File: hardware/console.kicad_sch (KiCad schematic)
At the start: 56 parts, among them J1 USB-C_Module, J3 SWD, J4 UART, J5 LiPo_140mAh, SW1 SW_LEFT, SW10 SW_BOOT0, SW2 SW_RIGHT, SW3 SW_UP, SW4 SW_DOWN, SW5 SW_A, SW6 SW_B, SW7 SW_POWER, SW8 SW_START, SW9 SW_SELECT, U1 STM32G0B1CBT6, U2 XC6206P332MR, U3 TP4054

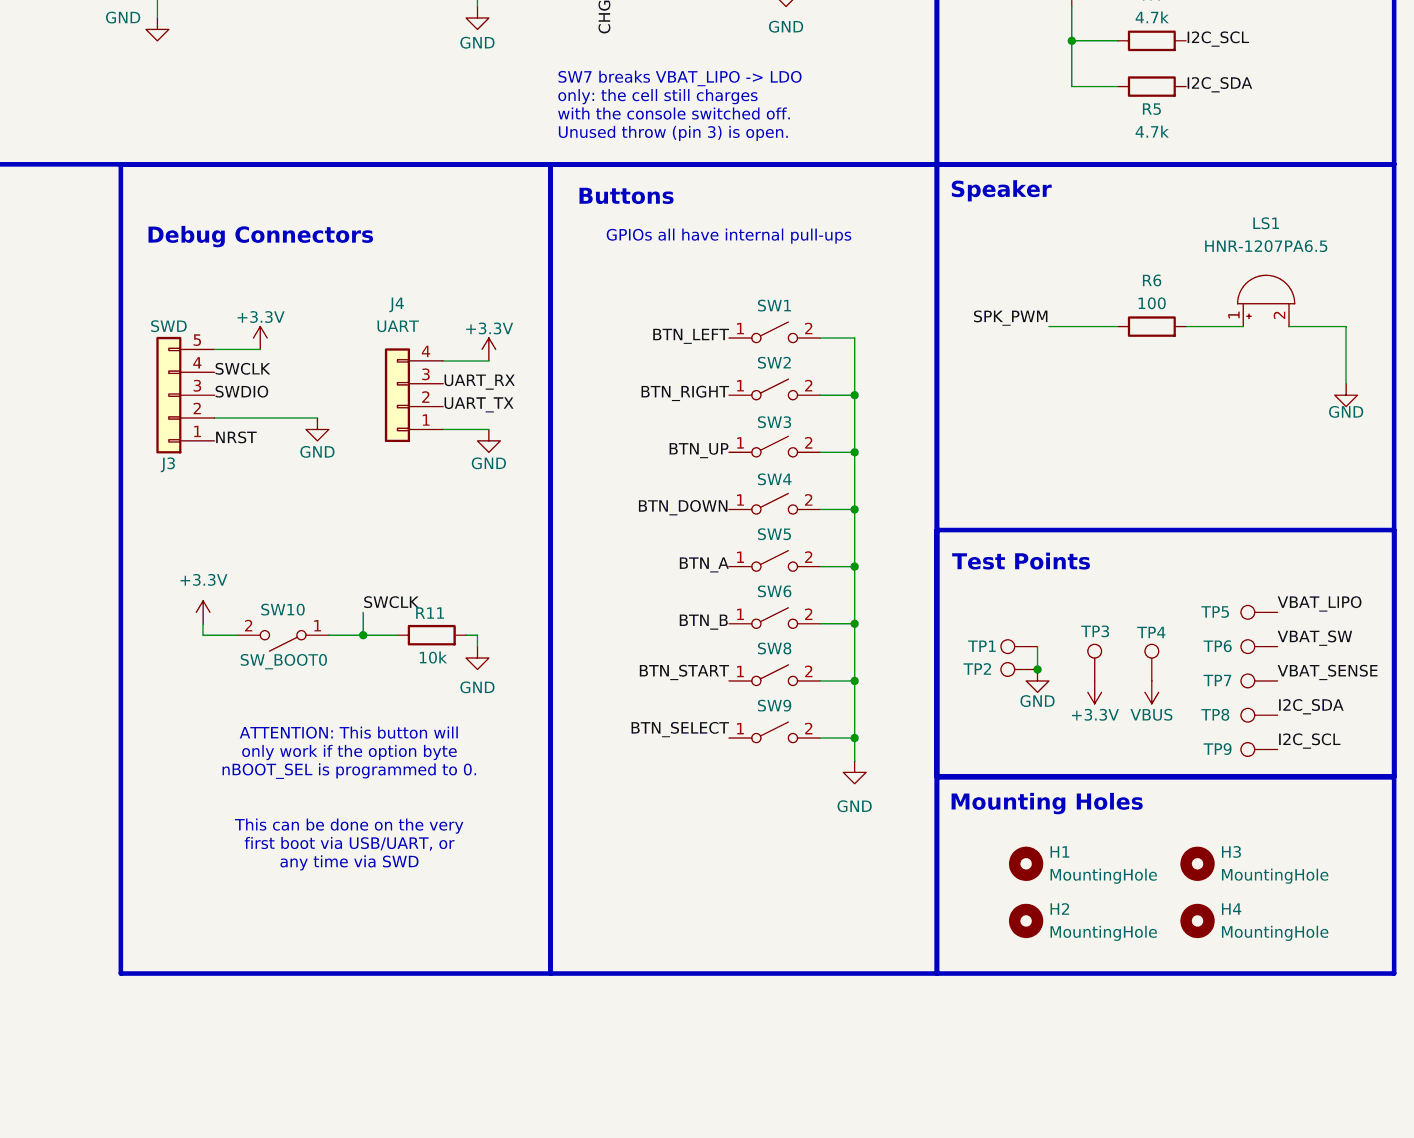
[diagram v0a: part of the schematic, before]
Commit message: remove the boot0 btn
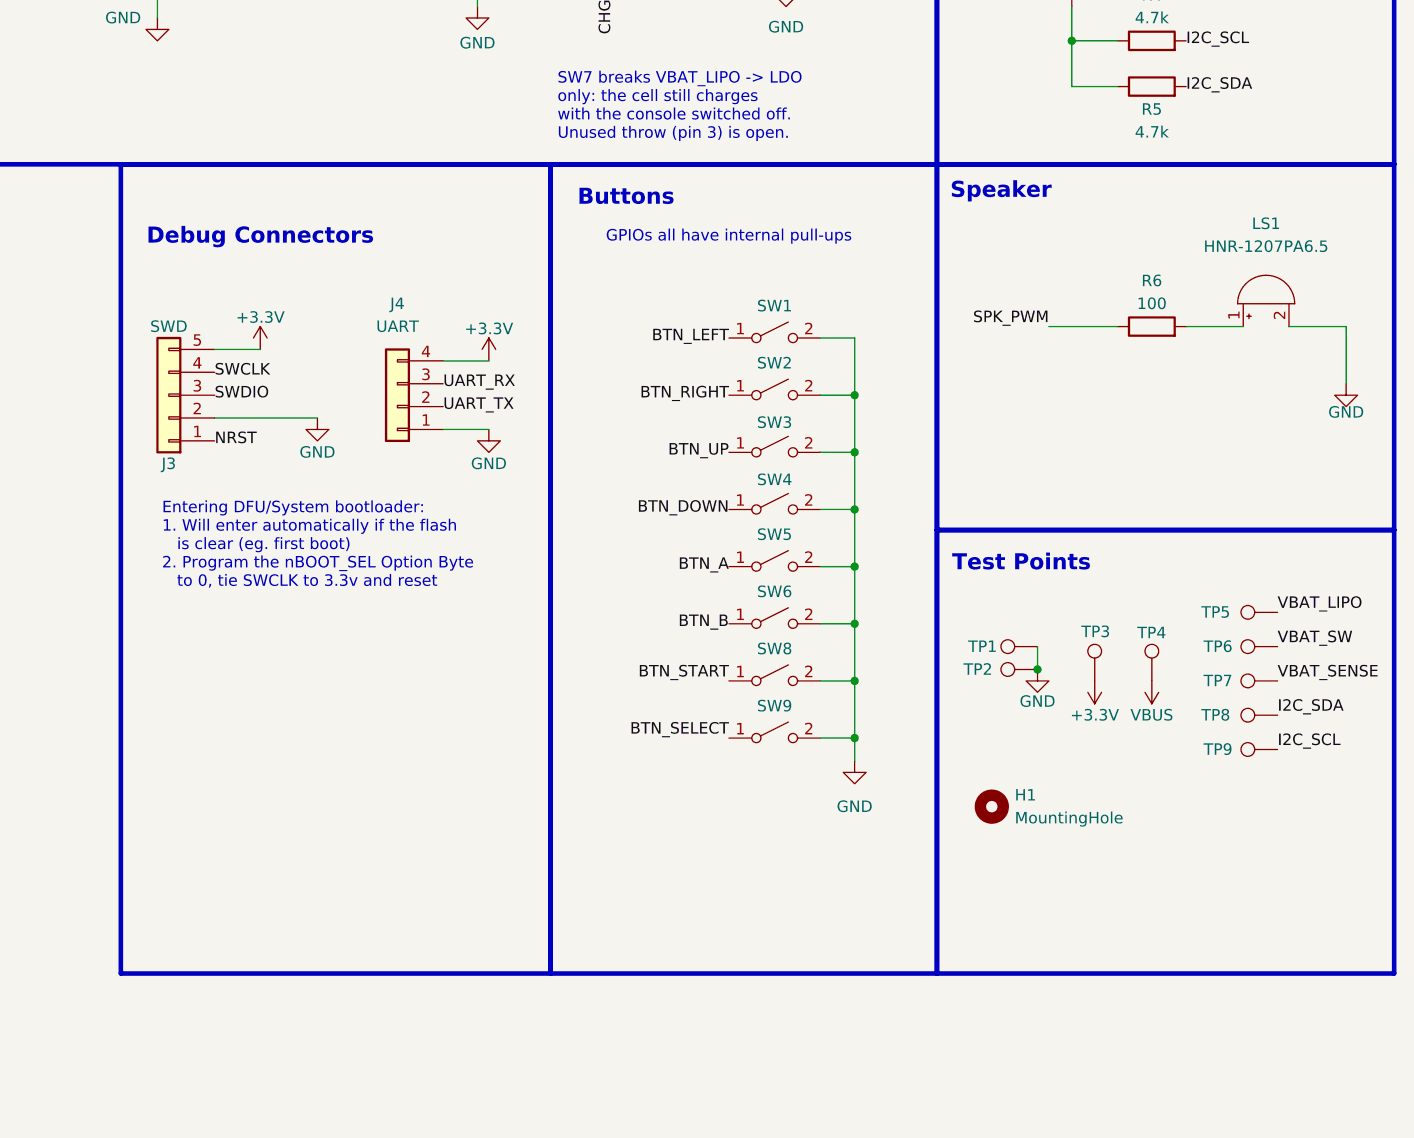
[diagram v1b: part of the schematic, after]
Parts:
- removed H2, H3, H4: MountingHole, MountingHole:MountingHole_2.5mm, symbol Mechanical:MountingHole
- removed R11: 10k, Resistor_SMD:R_0402_1005Metric, symbol Device:R
- removed SW10: SW_BOOT0, Button_Switch_SMD:SW_SPST_TS-1088-xR020, symbol Switch:SW_SPST
- H1: footprint MountingHole:MountingHole_2.5mm -> MountingHole:MountingHole_2.1mm
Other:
- note added: "Entering DFU/System bootloader: 1. Will enter automatically if the flash is clear (eg. first boot) 2. Program the nBOOT_SEL Option Byte to 0, tie SWCLK to 3.3v and reset"
- note removed: "ATTENTION: This button will only work if the option byte nBOOT_SEL is programmed to 0. This can be done on the very first boot via USB/UART, or any time via SWD"
- note removed: "Mounting Holes"
- moved on the sheet: H1

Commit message: footprint for usb module, and a AI-generated 3d model
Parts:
- J1: footprint Connector_PinHeader_2.54mm:PinHeader_1x06_P2.54mm_Vertical -> console:USBC-TH_L21.6-W12.8-P2.54
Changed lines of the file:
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@@
 			)
 		)
-		(property "Footprint" "Connector_PinHeader_2.54mm:PinHeader_1x06_P2.54mm_Vertical"
+		(property "Footprint" "console:USBC-TH_L21.6-W12.8-P2.54"
 			(at 22.86 40.64 0)
 			(hide yes)

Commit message: change some components to be manually soldered
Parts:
- DS1, J3, J4, J5, SW7: now left out of the parts list
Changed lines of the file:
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@@
 		(body_style 1)
 		(exclude_from_sim no)
-		(in_bom yes)
+		(in_bom no)
 		(on_board yes)
 		(in_pos_files yes)
@@
 		(body_style 1)
 		(exclude_from_sim no)
-		(in_bom yes)
+		(in_bom no)
 		(on_board yes)
 		(in_pos_files yes)
@@
 		(body_style 1)
 		(exclude_from_sim no)
-		(in_bom yes)
+		(in_bom no)
 		(on_board yes)
 		(in_pos_files yes)
@@
 		(body_style 1)
 		(exclude_from_sim no)
-		(in_bom yes)
+		(in_bom no)
 		(on_board yes)
 		(in_pos_files yes)
@@
 		(body_style 1)
 		(exclude_from_sim no)
-		(in_bom yes)
+		(in_bom no)
 		(on_board yes)
 		(in_pos_files yes)

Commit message: change the mcu ... again
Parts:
- U1: value STM32G0B1CBT6 -> STM32G070CBT6; symbol MCU_ST_STM32G0:STM32G0B1CBTx -> MCU_ST_STM32G0:STM32G070CBTx; LCSC C2847904 -> C529338; MPN STM32G0B1CBT6 -> STM32G070CBT6
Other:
- note removed: "Entering DFU/System bootloader: 1. Will enter automatically if the flash is clear (eg. first boot) 2. Program the nBOOT_SEL Option Byte to 0, tie SWCLK to 3.3v and reset"
- moved on the sheet: C7, C8, C9

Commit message: pushbutton values
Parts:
- SW1: value SW_LEFT -> SW_PUSH
- SW2: value SW_RIGHT -> SW_PUSH
- SW3: value SW_UP -> SW_PUSH
- SW4: value SW_DOWN -> SW_PUSH
- SW5: value SW_A -> SW_PUSH
- SW6: value SW_B -> SW_PUSH
- SW8: value SW_START -> SW_PUSH
- SW9: value SW_SELECT -> SW_PUSH
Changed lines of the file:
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@@
 			)
 		)
-		(property "Value" "SW_START"
+		(property "Value" "SW_PUSH"
 			(at 215.9 129.54 0)
 			(hide yes)
@@
 			)
 		)
-		(property "Value" "SW_SELECT"
+		(property "Value" "SW_PUSH"
 			(at 215.9 135.89 0)
 			(hide yes)
@@
 			)
 		)
-		(property "Value" "SW_UP"
+		(property "Value" "SW_PUSH"
 			(at 215.9 104.14 0)
 			(hide yes)
@@
 			)
 		)
-		(property "Value" "SW_DOWN"
+		(property "Value" "SW_PUSH"
 			(at 215.9 110.49 0)
 			(hide yes)
@@
 			)
 		)
-		(property "Value" "SW_LEFT"
+		(property "Value" "SW_PUSH"
 			(at 215.9 91.44 0)
 			(hide yes)
@@
 			)
 		)
-		(property "Value" "SW_RIGHT"
+		(property "Value" "SW_PUSH"
 			(at 215.9 97.79 0)
 			(hide yes)
@@
 			)
 		)
-		(property "Value" "SW_A"
+		(property "Value" "SW_PUSH"
 			(at 215.9 116.84 0)
 			(hide yes)
@@
 			)
 		)
-		(property "Value" "SW_B"
+		(property "Value" "SW_PUSH"
 			(at 215.9 123.19 0)
 			(hide yes)

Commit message: delete more stuff
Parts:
- removed TP3: +3.3V, TestPoint:TestPoint_THTPad_D1.5mm_Drill0.7mm, symbol Connector:TestPoint
- removed TP4: VBUS, TestPoint:TestPoint_THTPad_D1.5mm_Drill0.7mm, symbol Connector:TestPoint
- removed TP8: I2C_SDA, TestPoint:TestPoint_THTPad_D1.5mm_Drill0.7mm, symbol Connector:TestPoint
- removed TP9: I2C_SCL, TestPoint:TestPoint_THTPad_D1.5mm_Drill0.7mm, symbol Connector:TestPoint

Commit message: move switch and chrg led to the top right
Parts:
- removed TP1: GND, TestPoint:TestPoint_Loop_D2.50mm_Drill1.0mm, symbol Connector:TestPoint
- removed TP2: GND, TestPoint:TestPoint_THTPad_D1.5mm_Drill0.7mm, symbol Connector:TestPoint
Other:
- moved on the sheet: TP5, TP6, TP7
